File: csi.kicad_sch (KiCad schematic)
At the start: 22 parts, among them J601 Conn_FFC_WE_68715014522, U601 AP22615A_TSOT26, U602 AP22615A_TSOT26

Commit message: [#63565] Synchronize components with library, bump revision to 1.0.4
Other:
- company: Antmicro -> Antmicro Ltd
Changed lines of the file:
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@@
   (title_block
     (title "CM4 Baseboard")
-    (date "2024-06-19")
-    (rev "1.0.3")
-    (company "Antmicro")
+    (date "2024-08-02")
+    (rev "1.0.5")
+    (company "Antmicro Ltd")
     (comment 1 "www.antmicro.com")
   )

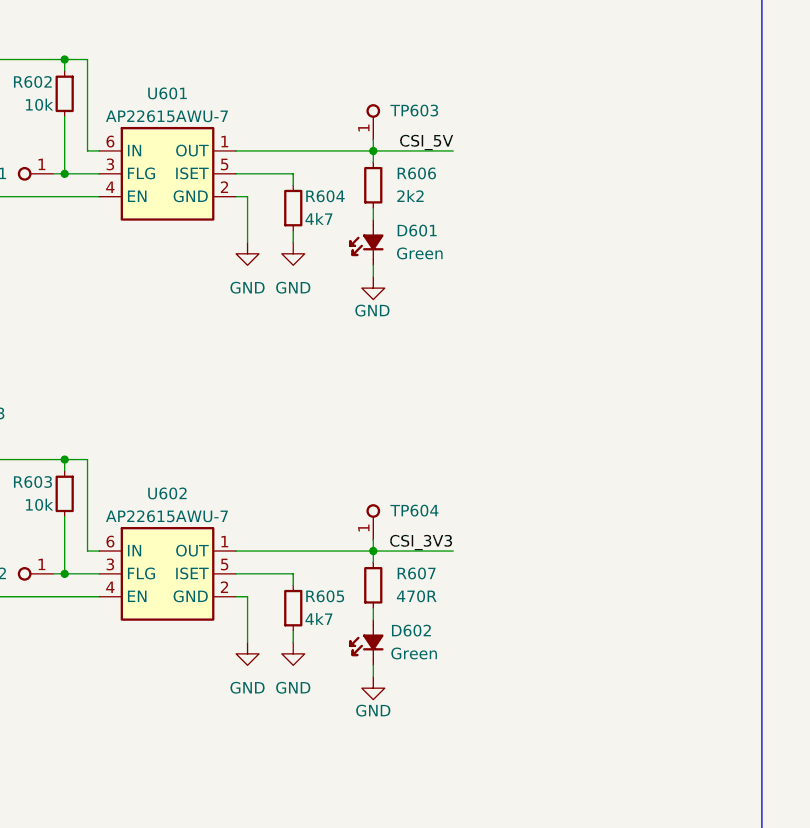
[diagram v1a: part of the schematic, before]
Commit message: [#65638] Fix green LEDs, bump revision to 1.0.5
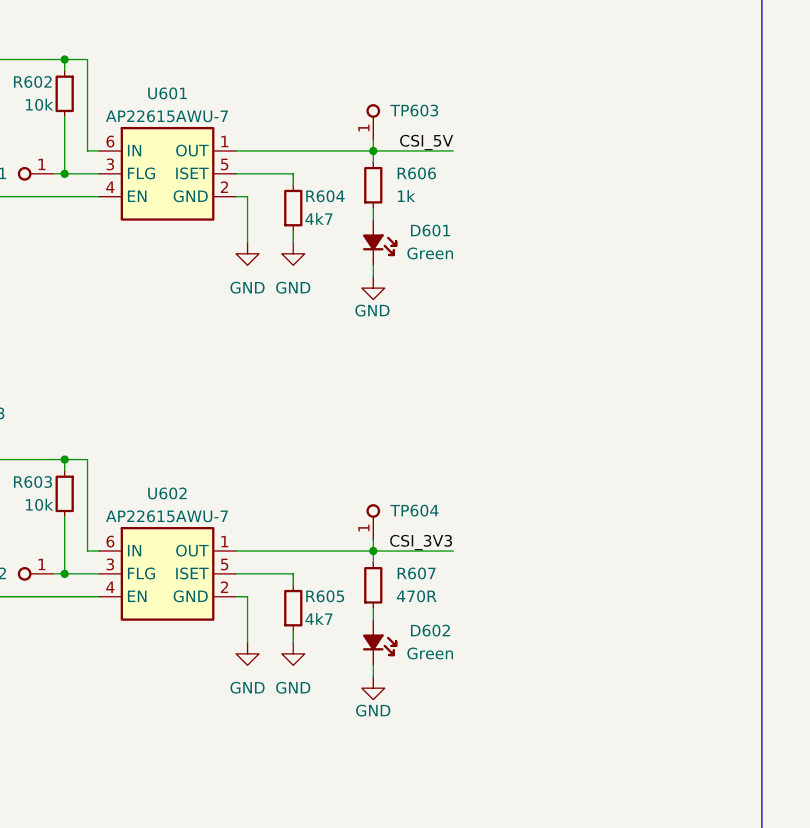
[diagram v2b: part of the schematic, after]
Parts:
- removed D601, D602: LED_G_0603_598-8D80-107F, antmicro-footprints:LED_0603_1608Metric_G, symbol antmicroLEDIndicationDiscrete:LED_G_0603_598-8D80-107F
- removed R606: R_2k2_0402, antmicro-footprints:R_0402_1005Metric, symbol antmicroResistors0402:R_2k2_0402
- added D601, D602: LED_G_0603_KP-1608CGCK, antmicro-footprints:LED_0603_1608Metric_G, symbol antmicroLEDIndicationDiscrete:LED_G_0603_KP-1608CGCK
- added R606: R_1k_0402, antmicro-footprints:R_0402_1005Metric, symbol antmicroResistors0402:R_1k_0402
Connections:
- net CSI_5V: now also R606.2
- net GND: now also D601.1 (C), D602.1 (C)
- net at R607.1: now also D602.2 (A)
- new net: D601.2 (A), R606.1
